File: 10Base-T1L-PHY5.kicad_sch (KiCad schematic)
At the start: 53 parts, among them J7 PHY0_MDI, U10 ADIN1100, U2 SJA1105Q

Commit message: Minor corrections
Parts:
- added R151: 4K7, Resistor_SMD:R_0603_1608Metric, symbol Device:R
- R152: renamed from R146; value 1K -> 4K7
- R153: renamed from R147; value 1K -> 4K7
- renumbered R142 to R147, R143 to R148, R144 to R149, R145 to R150, R148 to R154, R149 to R155, R150 to R156, R151 to R157, R152 to R158, R153 to R159, R154 to R160, R155 to R161, R156 to R162, R157 to R163, R158 to R164, R159 to R165, R160 to R166, R161 to R167, R162 to R168, R163 to R169, R164 to R170, R165 to R171, R166 to R172, R167 to R173
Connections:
- net +3V3: now also R151.2
- net at R156.1, U2.A11 (MII2_RX_DV): now also R151.1
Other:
- note added: "Config: ------ MACIF_SEL: 0b00 => RMII MS_SEL2: 0b0 => Prefer Slave TX2P4: 0b0 => Enable 1.0V and 2.4V TX SWPD_ENB: 0b1 => Do not enter power down"

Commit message: Assigning Footprints
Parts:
- added C267: 8p2, Capacitor_SMD:C_0603_1608Metric, symbol Device:C
- added C268: 10p, Capacitor_SMD:C_0603_1608Metric, symbol Device:C
- D28: footprint (none) -> Diode_SMD:D_SOD-323
- D29, D30: footprint (none) -> UCLAMP3311P:SLP1006P2
- FB14: footprint Inductor_SMD:L_0805_2012Metric -> Inductor_SMD:L_1206_3216Metric
- H6: footprint (none) -> MountingHole:MountingHole_3.2mm_M3_Pad_Via
- J7: value PHY0_MDI -> PHY5_MDI; footprint (none) -> TerminalBlock_RND:TerminalBlock_RND_205-00288_1x03_P5.08mm_Horizontal
- L18: footprint (none) -> PID75:PID75-251M
- L19, L20: footprint (none) -> ICI70CGI:ICI70CGI
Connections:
- net GND: now also C268.2
- net at U10.8 (XTAL_I/CLK_IN): now also C267.2, C268.1; no longer R163.2
- new net: C267.1, R163.2
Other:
- note added: "1Vp-p attenuation"
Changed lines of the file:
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@@
   (junction (at 213.36 62.23) (diameter 0) (color 0 0 0 0)
   )
+  (junction (at 55.88 102.87) (diameter 0) (color 0 0 0 0)
+  )
   (junction (at 49.53 66.04) (diameter 0) (color 0 0 0 0)
   )
@@
     (stroke (width 0) (type default) (color 0 0 0 0))
   )
-  (wire (pts (xy 49.53 83.82) (xy 68.58 83.82))
+  (wire (pts (xy 49.53 83.82) (xy 55.88 83.82))
     (stroke (width 0) (type default) (color 0 0 0 0))
   )
@@
     (stroke (width 0) (type default) (color 0 0 0 0))
   )
-  (wire (pts (xy 68.58 83.82) (xy 68.58 106.68))
-    (stroke (width 0) (type default) (color 0 0 0 0))
-  )
   (wire (pts (xy 203.2 53.34) (xy 200.66 53.34))
     (stroke (width 0) (type default) (color 0 0 0 0))
@@
     (stroke (width 0) (type default) (color 0 0 0 0))
   )
+  (wire (pts (xy 55.88 102.87) (xy 68.58 102.87))
+    (stroke (width 0) (type default) (color 0 0 0 0))
+  )
   (wire (pts (xy 41.91 68.58) (xy 69.85 68.58))
     (stroke (width 0) (type default) (color 0 0 0 0))
@@
     (stroke (width 0) (type default) (color 0 0 0 0))
   )
+  (wire (pts (xy 55.88 83.82) (xy 55.88 95.25))
+    (stroke (width 0) (type default) (color 0 0 0 0))
+  )
   (wire (pts (xy 147.32 132.08) (xy 154.94 132.08))
     (stroke (width 0) (type default) (color 0 0 0 0))
@@
   )
   (wire (pts (xy 149.86 58.42) (xy 149.86 63.5))
+    (stroke (width 0) (type default) (color 0 0 0 0))
+  )
+  (wire (pts (xy 68.58 102.87) (xy 68.58 106.68))
     (stroke (width 0) (type default) (color 0 0 0 0))
   )
@@
   )
   (text "Hybrid according to\nADIN1100 Datasheet" (at 137.16 54.61 0)
+    (effects (font (size 1.27 1.27)) (justify left bottom))
+  )
+  (text "1Vp-p\nattenuation" (at 60.96 101.6 0)
     (effects (font (size 1.27 1.27)) (justify left bottom))
   )
@@
     (property "Reference" "H6" (id 0) (at 279.4 87.63 0))
     (property "Value" "CHASSIS_PE" (id 1) (at 277.495 87.63 0))
-    (property "Footprint" "" (id 2) (at 273.05 87.63 0)
+    (property "Footprint" "MountingHole:MountingHole_3.2mm_M3_Pad_Via" (id 2) (at 273.05 87.63 0)
       (effects (font (size 1.27 1.27)) hide)
     )
@@
     (property "Reference" "D30" (id 0) (at 168.91 93.98 0))
     (property "Value" "UCLAMP3311P" (id 1) (at 180.34 93.98 90))
-    (property "Footprint" "" (id 2) (at 171.45 93.98 0)
+    (property "Footprint" "UCLAMP3311P:SLP1006P2" (id 2) (at 171.45 93.98 0)
       (effects (font (size 1.27 1.27)) hide)
     )
@@
     (property "Reference" "L20" (id 0) (at 224.79 66.675 0))
     (property "Value" "RCM70CGI-471" (id 1) (at 224.79 77.47 0))
-    (property "Footprint" "" (id 2) (at 224.79 71.12 0)
-      (effects (font (size 1.27 1.27)) hide)
-    )
-    (property "Datasheet" "~" (id 3) (at 224.79 71.12 0)
+    (property "Footprint" "ICI70CGI:ICI70CGI" (id 2) (at 224.79 71.12 0)
+      (effects (font (size 1.27 1.27)) hide)
+    )
+    (property "Datasheet" "https://product.tdk.com/system/files/dam/doc/product/transformer/transformer/lan/data_sheet/30/ds/lan_mod/rcm70cgi.pdf" (id 3) (at 224.79 71.12 0)
       (effects (font (size 1.27 1.27)) hide)
     )
@@
     (property "Reference" "L18" (id 0) (at 230.505 53.34 0))
     (property "Value" "PID75-251M" (id 1) (at 239.395 53.34 0))
-    (property "Footprint" "" (id 2) (at 234.95 53.34 0)
-      (effects (font (size 1.27 1.27)) hide)
-    )
-    (property "Datasheet" "~" (id 3) (at 234.95 53.34 0)
+    (property "Footprint" "PID75:PID75-251M" (id 2) (at 234.95 53.34 0)
+      (effects (font (size 1.27 1.27)) hide)
+    )
+    (property "Datasheet" "https://product.tdk.com/system/files/dam/doc/product/inductor/inductor/smd/data_sheet/30/db/ind_2008/pidx251m.pdf" (id 3) (at 234.95 53.34 0)
       (effects (font (size 1.27 1.27)) hide)
     )
@@
     (pin "2")
   )
+  (symbol (lib_id "power:GND") (at 55.88 110.49 0) (unit 1)
+    (in_bom yes) (on_board yes)
+    (property "Reference" "#PWR0253" (id 0) (at 55.88 116.84 0)
+      (effects (font (size 1.27 1.27)) hide)
+    )
+    (property "Value" "GND" (id 1) (at 55.88 114.3 0))
+    (property "Footprint" "" (id 2) (at 55.88 110.49 0)
+      (effects (font (size 1.27 1.27)) hide)
+    )
+    (property "Datasheet" "" (id 3) (at 55.88 110.49 0)
+      (effects (font (size 1.27 1.27)) hide)
+    )
+    (pin "1")
+  )
   (symbol (lib_id "Device:C") (at 179.07 62.23 90) (unit 1)
     (in_bom yes) (on_board yes)
@@
     (property "Reference" "D28" (id 0) (at 248.92 71.12 0))
     (property "Value" "CDSOD323-T36SC" (id 1) (at 251.46 63.5 90))
-    (property "Footprint" "" (id 2) (at 251.46 71.12 0)
+    (property "Footprint" "Diode_SMD:D_SOD-323" (id 2) (at 251.46 71.12 0)
       (effects (font (size 1.27 1.27)) hide)
     )
@@
     (property "Reference" "D29" (id 0) (at 163.83 93.98 0))
     (property "Value" "UCLAMP3311P" (id 1) (at 156.21 93.98 90))
-    (property "Footprint" "" (id 2) (at 166.37 93.98 0)
+    (property "Footprint" "UCLAMP3311P:SLP1006P2" (id 2) (at 166.37 93.98 0)
       (effects (font (size 1.27 1.27)) hide)
     )
@@
     (pin "2")
   )
+  (symbol (lib_id "Device:C") (at 55.88 106.68 0) (unit 1)
+    (in_bom yes) (on_board yes)
+    (property "Reference" "C268" (id 0) (at 56.515 104.14 0)
+      (effects (font (size 1.27 1.27)) (justify left))
+    )
+    (property "Value" "10p" (id 1) (at 56.515 109.22 0)
+      (effects (font (size 1.27 1.27)) (justify left))
+    )
+    (property "Footprint" "Capacitor_SMD:C_0603_1608Metric" (id 2) (at 56.8452 110.49 0)
+      (effects (font (size 1.27 1.27)) hide)
+    )
+    (property "Datasheet" "~" (id 3) (at 55.88 106.68 0)
+      (effects (font (size 1.27 1.27)) hide)
+    )
+    (pin "1")
+    (pin "2")
+  )
   (symbol (lib_id "Device:R") (at 45.72 83.82 90) (unit 1)
     (in_bom yes) (on_board yes)
@@
     (property "Reference" "FB14" (id 0) (at 161.925 113.03 90))
     (property "Value" "FerriteBead" (id 1) (at 162.56 105.41 90))
-    (property "Footprint" "Inductor_SMD:L_0805_2012Metric" (id 2) (at 162.56 110.998 90)
+    (property "Footprint" "Inductor_SMD:L_1206_3216Metric" (id 2) (at 162.56 110.998 90)
       (effects (font (size 1.27 1.27)) hide)
     )
@@
     )
     (property "Datasheet" "~" (id 3) (at 115.57 124.46 0)
+      (effects (font (size 1.27 1.27)) hide)
+    )
+    (pin "1")
+    (pin "2")
+  )
+  (symbol (lib_id "Device:C") (at 55.88 99.06 0) (unit 1)
+    (in_bom yes) (on_board yes)
+    (property "Reference" "C267" (id 0) (at 56.515 96.52 0)
+      (effects (font (size 1.27 1.27)) (justify left))
+    )
+    (property "Value" "8p2" (id 1) (at 56.515 101.6 0)
+      (effects (font (size 1.27 1.27)) (justify left))
+    )
+    (property "Footprint" "Capacitor_SMD:C_0603_1608Metric" (id 2) (at 56.8452 102.87 0)
+      (effects (font (size 1.27 1.27)) hide)
+    )
+    (property "Datasheet" "~" (id 3) (at 55.88 99.06 0)
       (effects (font (size 1.27 1.27)) hide)
     )
@@
     (property "Reference" "L19" (id 0) (at 192.405 71.12 0))
     (property "Value" "ICI70CGI-222" (id 1) (at 179.07 71.12 90))
-    (property "Footprint" "" (id 2) (at 187.96 71.12 0)
-      (effects (font (size 1.27 1.27)) hide)
-    )
-    (property "Datasheet" "~" (id 3) (at 187.96 71.12 0)
+    (property "Footprint" "ICI70CGI:ICI70CGI" (id 2) (at 187.96 71.12 0)
+      (effects (font (size 1.27 1.27)) hide)
+    )
+    (property "Datasheet" "https://product.tdk.com/system/files/dam/doc/product/transformer/transformer/lan/data_sheet/30/ds/lan_mod/ici70cgi.pdf" (id 3) (at 187.96 71.12 0)
       (effects (font (size 1.27 1.27)) hide)
     )
@@
     (in_bom yes) (on_board yes)
     (property "Reference" "J7" (id 0) (at 267.97 67.31 0))
-    (property "Value" "PHY0_MDI" (id 1) (at 267.97 77.47 0))
-    (property "Footprint" "" (id 2) (at 267.97 72.39 0)
-      (effects (font (size 1.27 1.27)) hide)
-    )
+    (property "Value" "PHY5_MDI" (id 1) (at 267.97 77.47 0))
+    (property "Footprint" "TerminalBlock_RND:TerminalBlock_RND_205-00288_1x03_P5.08mm_Horizontal" (id 2) (at 267.97 72.39 0)
+      (effects (font (size 1.27 1.27)) hide)
+    )

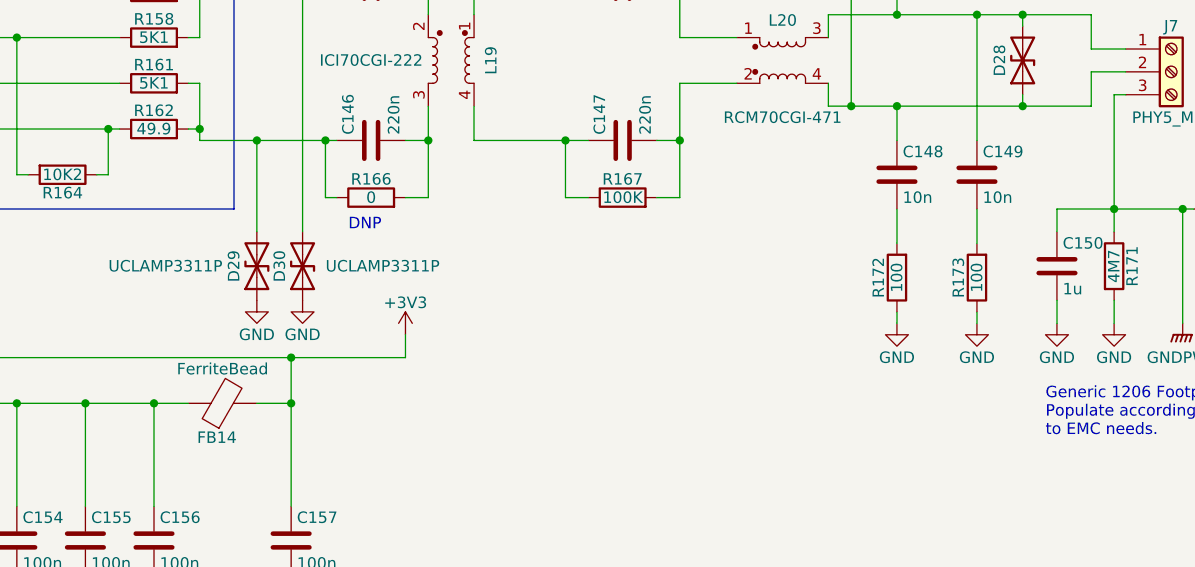
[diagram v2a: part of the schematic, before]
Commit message: Fixing termination for T1L PHYs
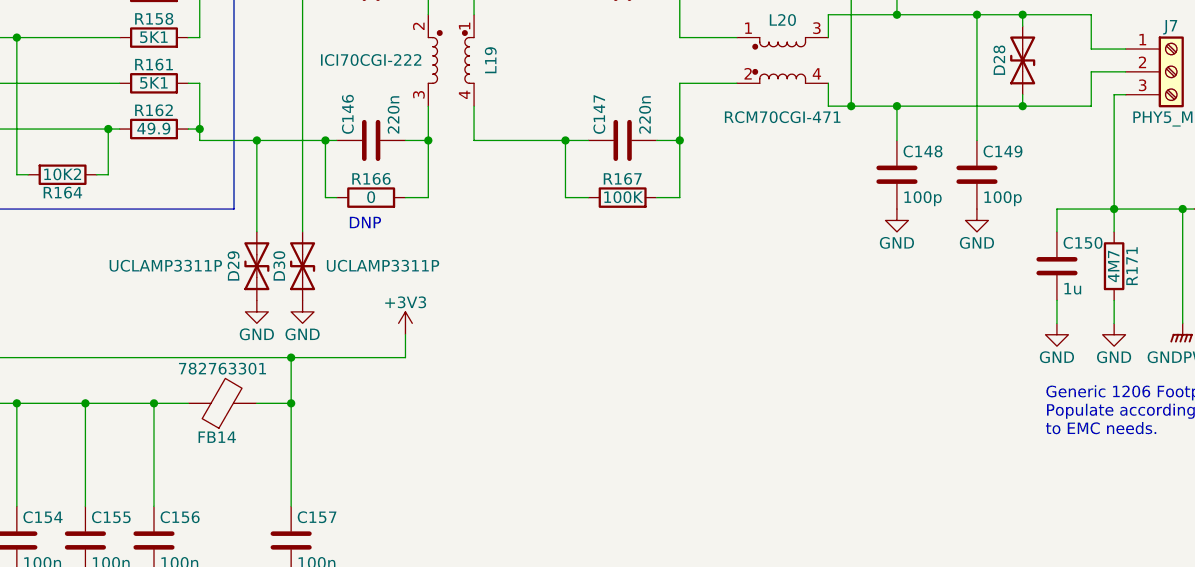
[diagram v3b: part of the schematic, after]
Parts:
- removed R172, R173: 100, Resistor_SMD:R_0805_2012Metric, symbol Device:R
- C148, C149: value 10n -> 100p
- FB14: value FerriteBead -> 782763301
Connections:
- net GND: now also C148.2, C149.2
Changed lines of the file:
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@@
-    (stroke (width 0) (type default) (color 0 0 0 0))
-  )
-  (wire (pts (xy 237.49 87.63) (xy 237.49 91.44))
     (stroke (width 0) (type default) (color 0 0 0 0))
   )
@@
     (stroke (width 0) (type default) (color 0 0 0 0))
   )
-  (wire (pts (xy 237.49 99.06) (xy 237.49 100.33))
-    (stroke (width 0) (type default) (color 0 0 0 0))
-  )
   (wire (pts (xy 200.66 80.01) (xy 203.2 80.01))
     (stroke (width 0) (type default) (color 0 0 0 0))
@@
     (stroke (width 0) (type default) (color 0 0 0 0))
   )
-  (wire (pts (xy 246.38 87.63) (xy 246.38 91.44))
-    (stroke (width 0) (type default) (color 0 0 0 0))
-  )
   (wire (pts (xy 229.87 76.2) (xy 229.87 73.66))
     (stroke (width 0) (type default) (color 0 0 0 0))
@@
   )
   (wire (pts (xy 132.08 128.27) (xy 132.08 132.08))
-    (stroke (width 0) (type default) (color 0 0 0 0))
-  )
-  (wire (pts (xy 246.38 99.06) (xy 246.38 100.33))
     (stroke (width 0) (type default) (color 0 0 0 0))
   )
@@
       (effects (font (size 1.27 1.27)) (justify left))
     )
-    (property "Value" "10n" (id 1) (at 247.015 86.36 0)
+    (property "Value" "100p" (id 1) (at 247.015 86.36 0)
       (effects (font (size 1.27 1.27)) (justify left))
     )
@@
     )
     (property "Datasheet" "~" (id 3) (at 45.72 93.98 0)
-      (effects (font (size 1.27 1.27)) hide)
-    )
-    (pin "1")
-    (pin "2")
-  )
-  (symbol (lib_id "Device:R") (at 246.38 95.25 180) (unit 1)
-    (in_bom yes) (on_board yes)
-    (property "Reference" "R173" (id 0) (at 244.348 95.25 90))
-    (property "Value" "100" (id 1) (at 246.38 95.25 90))
-    (property "Footprint" "Resistor_SMD:R_0805_2012Metric" (id 2) (at 248.158 95.25 90)
-      (effects (font (size 1.27 1.27)) hide)
-    )
-    (property "Datasheet" "~" (id 3) (at 246.38 95.25 0)
       (effects (font (size 1.27 1.27)) hide)
     )
@@
     (pin "2")
   )
-  (symbol (lib_id "power:GND") (at 246.38 100.33 0) (unit 1)
-    (in_bom yes) (on_board yes)
-    (property "Reference" "#PWR0150" (id 0) (at 246.38 106.68 0)
-      (effects (font (size 1.27 1.27)) hide)
-    )
-    (property "Value" "GND" (id 1) (at 246.38 104.14 0))
-    (property "Footprint" "" (id 2) (at 246.38 100.33 0)
-      (effects (font (size 1.27 1.27)) hide)
-    )
-    (property "Datasheet" "" (id 3) (at 246.38 100.33 0)
+  (symbol (lib_id "power:GND") (at 246.38 87.63 0) (unit 1)
+    (in_bom yes) (on_board yes)
+    (property "Reference" "#PWR0150" (id 0) (at 246.38 93.98 0)
+      (effects (font (size 1.27 1.27)) hide)
+    )
+    (property "Value" "GND" (id 1) (at 246.38 91.44 0))
+    (property "Footprint" "" (id 2) (at 246.38 87.63 0)
+      (effects (font (size 1.27 1.27)) hide)
+    )
+    (property "Datasheet" "" (id 3) (at 246.38 87.63 0)
       (effects (font (size 1.27 1.27)) hide)
     )
@@
     (in_bom yes) (on_board yes)
     (property "Reference" "FB14" (id 0) (at 161.925 113.03 90))
-    (property "Value" "FerriteBead" (id 1) (at 162.56 105.41 90))
+    (property "Value" "782763301" (id 1) (at 162.56 105.41 90))
     (property "Footprint" "Inductor_SMD:L_1206_3216Metric" (id 2) (at 162.56 110.998 90)
       (effects (font (size 1.27 1.27)) hide)
@@
     (pin "2")
   )
-  (symbol (lib_id "Device:R") (at 237.49 95.25 180) (unit 1)
-    (in_bom yes) (on_board yes)
-    (property "Reference" "R172" (id 0) (at 235.458 95.25 90))
-    (property "Value" "100" (id 1) (at 237.49 95.25 90))
-    (property "Footprint" "Resistor_SMD:R_0805_2012Metric" (id 2) (at 239.268 95.25 90)
-      (effects (font (size 1.27 1.27)) hide)
-    )
-    (property "Datasheet" "~" (id 3) (at 237.49 95.25 0)
-      (effects (font (size 1.27 1.27)) hide)
-    )
-    (pin "1")
-    (pin "2")
-  )
   (symbol (lib_id "Connector:Screw_Terminal_01x03") (at 267.97 72.39 0) (unit 1)
     (in_bom yes) (on_board yes)
@@
     (pin "1")
   )
-  (symbol (lib_id "power:GND") (at 237.49 100.33 0) (unit 1)
-    (in_bom yes) (on_board yes)
-    (property "Reference" "#PWR0149" (id 0) (at 237.49 106.68 0)
-      (effects (font (size 1.27 1.27)) hide)
-    )
-    (property "Value" "GND" (id 1) (at 237.49 104.14 0))
-    (property "Footprint" "" (id 2) (at 237.49 100.33 0)
-      (effects (font (size 1.27 1.27)) hide)
-    )
-    (property "Datasheet" "" (id 3) (at 237.49 100.33 0)
+  (symbol (lib_id "power:GND") (at 237.49 87.63 0) (unit 1)
+    (in_bom yes) (on_board yes)
+    (property "Reference" "#PWR0149" (id 0) (at 237.49 93.98 0)
+      (effects (font (size 1.27 1.27)) hide)
+    )
+    (property "Value" "GND" (id 1) (at 237.49 91.44 0))
+    (property "Footprint" "" (id 2) (at 237.49 87.63 0)
+      (effects (font (size 1.27 1.27)) hide)
+    )
+    (property "Datasheet" "" (id 3) (at 237.49 87.63 0)
       (effects (font (size 1.27 1.27)) hide)
     )
@@
       (effects (font (size 1.27 1.27)) (justify left))
     )
-    (property "Value" "10n" (id 1) (at 238.125 86.36 0)
-      (effects (font (size 1.27 1.27)) (justify left))
-    )
+    (property "Value" "100p" (id 1) (at 238.125 86.36 0)
+      (effects (font (size 1.27 1.27)) (justify left))
+    )
